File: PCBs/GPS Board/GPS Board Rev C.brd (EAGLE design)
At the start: 95.9 x 90.2 mm, 4 parts

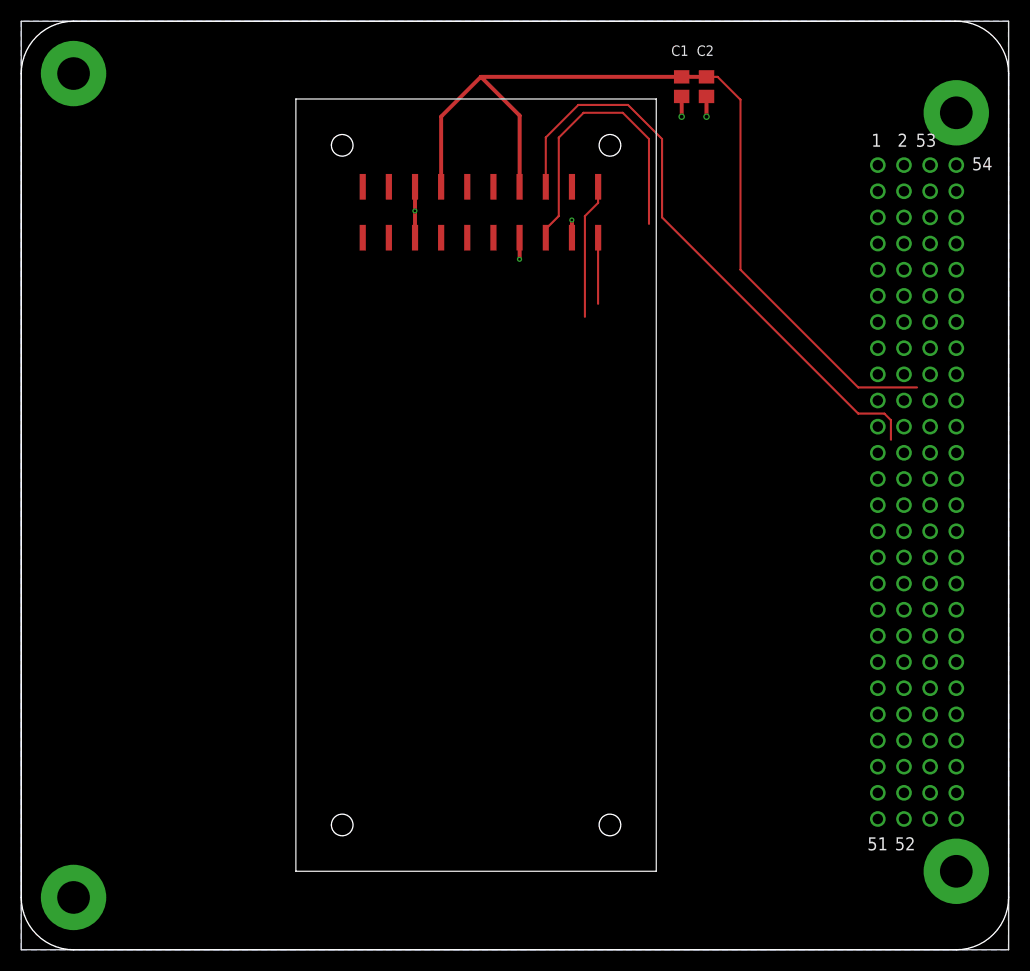
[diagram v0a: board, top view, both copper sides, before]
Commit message: Add test pads
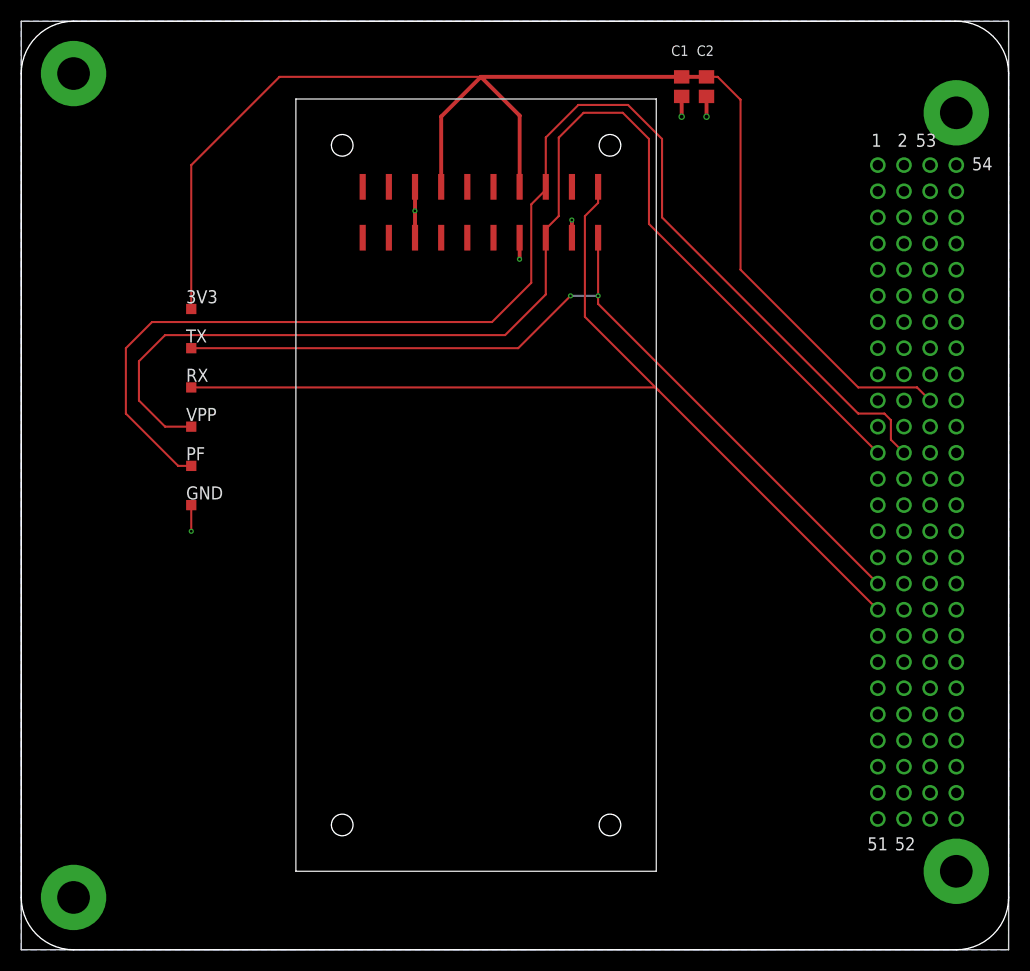
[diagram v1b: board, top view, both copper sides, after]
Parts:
- added 3V3, GND, PF, RX, TX, VPP: TPTP10SQ, testpad:TP10SQ
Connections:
- net GND: now also GND.TP
- net PF: now also PF.TP
- net RX: now also RX.TP
- net SW9: now also 3V3.TP
- net TX: now also TX.TP
- net VPP: now also VPP.TP
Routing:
- net VPP: track 29.3 -> 118.4 mm
- net RX: track 13.2 -> 98.9 mm
- net TX: track 6.43 -> 86.5 mm, vias 0 -> 2
- net PF: track 58.7 -> 127.2 mm
- net SW9: track 89.0 -> 136.5 mm
- net GND: track 12.7 -> 15.2 mm, vias 5 -> 6
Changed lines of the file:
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@@
 <element name="U$1" library="Cubesat" package="PINAV-L1" value="PINAV-L1" x="26.67" y="7.62"/>
 <element name="U$2" library="Cubesat" package="PC104_NO_DIMENSION" value="PC104_NO_DIMENSION" x="0" y="0"/>
+<element name="GND" library="testpad" library_urn="urn:adsk.eagle:library:385" package="TP10SQ" package3d_urn="urn:adsk.eagle:package:27962/1" value="TPTP10SQ" x="16.51" y="43.18">
+<attribute name="TP_SIGNAL_NAME" value="" x="16.51" y="43.18" size="1.778" layer="27" display="off"/>
+</element>
+<element name="TX" library="testpad" library_urn="urn:adsk.eagle:library:385" package="TP10SQ" package3d_urn="urn:adsk.eagle:package:27962/1" value="TPTP10SQ" x="16.51" y="58.42">
+<attribute name="TP_SIGNAL_NAME" value="" x="16.51" y="58.42" size="1.778" layer="27" display="off"/>
+</element>
+<element name="RX" library="testpad" library_urn="urn:adsk.eagle:library:385" package="TP10SQ" package3d_urn="urn:adsk.eagle:package:27962/1" value="TPTP10SQ" x="16.51" y="54.61">
+<attribute name="TP_SIGNAL_NAME" value="" x="16.51" y="54.61" size="1.778" layer="27" display="off"/>
+</element>
+<element name="3V3" library="testpad" library_urn="urn:adsk.eagle:library:385" package="TP10SQ" package3d_urn="urn:adsk.eagle:package:27962/1" value="TPTP10SQ" x="16.51" y="62.23">
+<attribute name="TP_SIGNAL_NAME" value="" x="16.51" y="62.23" size="1.778" layer="27" display="off"/>
+</element>
+<element name="VPP" library="testpad" library_urn="urn:adsk.eagle:library:385" package="TP10SQ" package3d_urn="urn:adsk.eagle:package:27962/1" value="TPTP10SQ" x="16.51" y="50.8">
+<attribute name="TP_SIGNAL_NAME" value="" x="16.51" y="50.8" size="1.778" layer="27" display="off"/>
+</element>
+<element name="PF" library="testpad" library_urn="urn:adsk.eagle:library:385" package="TP10SQ" package3d_urn="urn:adsk.eagle:package:27962/1" value="TPTP10SQ" x="16.51" y="46.99">
+<attribute name="TP_SIGNAL_NAME" value="" x="16.51" y="46.99" size="1.778" layer="27" display="off"/>
+</element>
 </elements>
 <signals>
@@
 <wire x1="86.995" y1="54.61" x2="81.28" y2="54.61" width="0.2032" layer="1"/>
 <contactref element="U$2" pad="71"/>
-<wire x1="88.265" y1="53.34" x2="86.995" y2="54.61" width="0" layer="19" extent="1-1"/>
+<wire x1="88.265" y1="53.34" x2="86.995" y2="54.61" width="0.2032" layer="1"/>
+<contactref element="3V3" pad="TP"/>
+<wire x1="44.638" y1="84.77" x2="25.08" y2="84.77" width="0.2032" layer="1"/>
+<wire x1="16.51" y1="76.2" x2="16.51" y2="62.23" width="0.2032" layer="1"/>
+<wire x1="25.08" y1="84.77" x2="16.51" y2="76.2" width="0.2032" layer="1"/>
 </signal>
 <signal name="GND">
@@
 <contactref element="U$2" pad="99"/>
 <contactref element="U$2" pad="100"/>
-<wire x1="64.135" y1="82.87" x2="66.548" y2="82.87" width="0" layer="19" extent="1-1"/>
-<wire x1="53.467" y1="70.866" x2="64.135" y2="80.899" width="0" layer="19" extent="1-1"/>
-<wire x1="48.4" y1="69.15" x2="53.48" y2="69.15" width="0" layer="19" extent="1-1"/>
-<wire x1="38.24" y1="69.15" x2="48.4" y2="69.15" width="0" layer="19" extent="1-1"/>
+<contactref element="GND" pad="TP"/>
+<wire x1="16.51" y1="43.18" x2="16.51" y2="40.64" width="0.2032" layer="1"/>
+<via x="16.51" y="40.64" extent="1-16" drill="0.254"/>
 <wire x1="38.227" y1="71.755" x2="38.24" y2="74.09" width="0" layer="19" extent="1-1"/>
-<wire x1="88.265" y1="66.04" x2="48.4" y2="67.069" width="0" layer="19" extent="1-1"/>
-<wire x1="90.805" y1="60.96" x2="88.265" y2="66.04" width="0" layer="19" extent="1-1"/>
-<wire x1="88.265" y1="55.88" x2="90.805" y2="60.96" width="0" layer="19" extent="1-1"/>
-<wire x1="88.265" y1="50.8" x2="88.265" y2="55.88" width="0" layer="19" extent="1-1"/>
-<wire x1="90.805" y1="50.8" x2="88.265" y2="50.8" width="0" layer="19" extent="1-1"/>
-<wire x1="90.805" y1="40.64" x2="90.805" y2="50.8" width="0" layer="19" extent="1-1"/>
-<wire x1="88.265" y1="40.64" x2="90.805" y2="40.64" width="0" layer="19" extent="1-1"/>
-<wire x1="90.805" y1="38.1" x2="90.805" y2="40.64" width="0" layer="19" extent="1-1"/>
-<wire x1="90.805" y1="17.78" x2="90.805" y2="38.1" width="0" layer="19" extent="1-1"/>
-<wire x1="88.265" y1="17.78" x2="90.805" y2="17.78" width="0" layer="19" extent="1-1"/>
 </signal>
 <signal name="VPP">
@@
 <wire x1="54.61" y1="81.28" x2="58.42" y2="81.28" width="0.2032" layer="1"/>
 <wire x1="58.42" y1="81.28" x2="60.96" y2="78.74" width="0.2032" layer="1"/>
-<wire x1="60.96" y1="78.74" x2="60.96" y2="70.485" width="0.2032" layer="1"/>
+<wire x1="60.96" y1="70.485" x2="60.96" y2="78.74" width="0.2032" layer="1"/>
 <wire x1="50.94" y1="69.99" x2="52.197" y2="71.247" width="0.2032" layer="1"/>
 <wire x1="52.197" y1="71.247" x2="52.197" y2="78.867" width="0.2032" layer="1"/>
 <wire x1="52.197" y1="78.867" x2="54.61" y2="81.28" width="0.2032" layer="1"/>
 <contactref element="U$2" pad="23"/>
-<wire x1="83.185" y1="48.26" x2="60.96" y2="70.485" width="0" layer="19" extent="1-1"/>
+<wire x1="83.185" y1="48.26" x2="60.96" y2="70.485" width="0.2032" layer="1"/>
+<contactref element="VPP" pad="TP"/>
+<wire x1="50.94" y1="69.15" x2="50.94" y2="63.64" width="0.2032" layer="1"/>
+<wire x1="50.94" y1="63.64" x2="46.99" y2="59.69" width="0.2032" layer="1"/>
+<wire x1="46.99" y1="59.69" x2="13.97" y2="59.69" width="0.2032" layer="1"/>
+<wire x1="13.97" y1="59.69" x2="11.43" y2="57.15" width="0.2032" layer="1"/>
+<wire x1="11.43" y1="53.34" x2="13.97" y2="50.8" width="0.2032" layer="1"/>
+<wire x1="13.97" y1="50.8" x2="16.51" y2="50.8" width="0.2032" layer="1"/>
+<wire x1="11.43" y1="57.15" x2="11.43" y2="53.34" width="0.2032" layer="1"/>
 </signal>
 <signal name="PF">
@@
 <wire x1="81.28" y1="52.07" x2="83.82" y2="52.07" width="0.2032" layer="1"/>
 <wire x1="83.82" y1="52.07" x2="84.455" y2="51.435" width="0.2032" layer="1"/>
-<wire x1="84.455" y1="51.435" x2="84.455" y2="49.53" width="0.2032" layer="1"/>
+<wire x1="84.455" y1="49.53" x2="84.455" y2="51.435" width="0.2032" layer="1"/>
 <wire x1="50.94" y1="78.88" x2="54.102" y2="82.042" width="0.2032" layer="1"/>
 <wire x1="54.102" y1="82.042" x2="58.928" y2="82.042" width="0.2032" layer="1"/>
@@
 <wire x1="62.23" y1="78.74" x2="62.23" y2="71.12" width="0.2032" layer="1"/>
 <contactref element="U$2" pad="24"/>
-<wire x1="85.725" y1="48.26" x2="84.455" y2="49.53" width="0" layer="19" extent="1-1"/>
+<wire x1="85.725" y1="48.26" x2="84.455" y2="49.53" width="0.2032" layer="1"/>
+<contactref element="PF" pad="TP"/>
+<wire x1="50.94" y1="74.09" x2="50.94" y2="73.8" width="0.2032" layer="1"/>
+<wire x1="50.94" y1="73.8" x2="49.53" y2="72.39" width="0.2032" layer="1"/>
+<wire x1="49.53" y1="64.77" x2="45.72" y2="60.96" width="0.2032" layer="1"/>
+<wire x1="12.7" y1="60.96" x2="10.16" y2="58.42" width="0.2032" layer="1"/>
+<wire x1="10.16" y1="58.42" x2="10.16" y2="52.07" width="0.2032" layer="1"/>
+<wire x1="10.16" y1="52.07" x2="15.24" y2="46.99" width="0.2032" layer="1"/>
+<wire x1="15.24" y1="46.99" x2="16.51" y2="46.99" width="0.2032" layer="1"/>
+<wire x1="49.53" y1="72.39" x2="49.53" y2="64.77" width="0.2032" layer="1"/>
+<wire x1="45.72" y1="60.96" x2="12.7" y2="60.96" width="0.2032" layer="1"/>
 </signal>
 <signal name="TX">
 <contactref element="U$1" pad="1"/>
-<wire x1="56.02" y1="69.15" x2="56.02" y2="62.725" width="0.2032" layer="1"/>
+<wire x1="56.02" y1="62.725" x2="56.02" y2="63.5" width="0.2032" layer="1"/>
 <contactref element="U$2" pad="33"/>
-<wire x1="83.185" y1="35.56" x2="56.02" y2="62.725" width="0" layer="19" extent="1-1"/>
+<wire x1="56.02" y1="63.5" x2="56.02" y2="69.15" width="0.2032" layer="1"/>
+<wire x1="83.185" y1="35.56" x2="56.02" y2="62.725" width="0.2032" layer="1"/>
+<contactref element="TX" pad="TP"/>
+<via x="56.02" y="63.5" extent="1-16" drill="0.254"/>
+<wire x1="56.02" y1="63.5" x2="53.34" y2="63.5" width="0.2032" layer="16"/>
+<via x="53.34" y="63.5" extent="1-16" drill="0.254"/>
+<wire x1="53.34" y1="63.5" x2="48.26" y2="58.42" width="0.2032" layer="1"/>
+<wire x1="48.26" y1="58.42" x2="16.51" y2="58.42" width="0.2032" layer="1"/>
 </signal>
 <signal name="RX">
@@
 <wire x1="56.02" y1="74.09" x2="56.02" y2="72.53" width="0.2032" layer="1"/>
 <wire x1="56.02" y1="72.53" x2="54.737" y2="71.247" width="0.2032" layer="1"/>
-<wire x1="54.737" y1="71.247" x2="54.737" y2="61.468" width="0.2032" layer="1"/>
+<wire x1="54.737" y1="61.468" x2="54.737" y2="71.247" width="0.2032" layer="1"/>
 <contactref element="U$2" pad="35"/>
-<wire x1="83.185" y1="33.02" x2="54.737" y2="61.468" width="0" layer="19" extent="1-1"/>
+<wire x1="83.185" y1="33.02" x2="61.9125" y2="54.2925" width="0.2032" layer="1"/>
+<contactref element="RX" pad="TP"/>
+<wire x1="61.9125" y1="54.2925" x2="54.737" y2="61.468" width="0.2032" layer="1"/>
+<wire x1="16.51" y1="54.61" x2="61.595" y2="54.61" width="0.2032" layer="1"/>
+<wire x1="61.595" y1="54.61" x2="61.9125" y2="54.2925" width="0.2032" layer="1"/>
 </signal>
 </signals>

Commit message: Rearrange pins to keep traces only on topside
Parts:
- moved PF 11.4 mm to (16.5, 58.4)
- moved TX 11.4 mm to (16.5, 47.0)
- moved RX 3.81 mm to (16.5, 50.8)
- moved VPP 3.81 mm to (16.5, 54.6)
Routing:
- net PF: track 127.2 -> 106.0 mm
- net VPP: track 118.4 -> 104.4 mm
- net RX: track 98.9 -> 106.1 mm
- net TX: track 86.5 -> 90.9 mm, vias 2 -> 0
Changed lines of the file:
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@@
 <setting verticaltext="up"/>
 </settings>
-<grid distance="50" unitdist="mil" unit="mil" style="lines" multiple="1" display="yes" altdistance="5" altunitdist="mil" altunit="mil"/>
+<grid distance="25" unitdist="mil" unit="mil" style="lines" multiple="1" display="yes" altdistance="5" altunitdist="mil" altunit="mil"/>
 <layers>
 <layer number="1" name="Top" color="4" fill="1" visible="yes" active="yes"/>
@@
 <layer number="43" name="vRestrict" color="2" fill="10" visible="yes" active="yes"/>
 <layer number="44" name="Drills" color="7" fill="1" visible="no" active="yes"/>
-<layer number="45" name="Holes" color="7" fill="1" visible="no" active="yes"/>
+<layer number="45" name="Holes" color="7" fill="1" visible="yes" active="yes"/>
 <layer number="46" name="Milling" color="3" fill="1" visible="no" active="yes"/>
 <layer number="47" name="Measures" color="7" fill="1" visible="no" active="yes"/>
@@
 <wire x1="0" y1="85.09" x2="5.08" y2="90.17" width="0.127" layer="20" curve="-90"/>
 <wire x1="5.08" y1="90.17" x2="90.678" y2="90.17" width="0.127" layer="20"/>
+<hole x="56.007" y="71.12" drill="0.35"/>
 </plain>
 <attributes>
@@
 <attribute name="TP_SIGNAL_NAME" value="" x="16.51" y="43.18" size="1.778" layer="27" display="off"/>
 </element>
-<element name="TX" library="testpad" library_urn="urn:adsk.eagle:library:385" package="TP10SQ" package3d_urn="urn:adsk.eagle:package:27962/1" value="TPTP10SQ" x="16.51" y="58.42">
-<attribute name="TP_SIGNAL_NAME" value="" x="16.51" y="58.42" size="1.778" layer="27" display="off"/>
-</element>
-<element name="RX" library="testpad" library_urn="urn:adsk.eagle:library:385" package="TP10SQ" package3d_urn="urn:adsk.eagle:package:27962/1" value="TPTP10SQ" x="16.51" y="54.61">
-<attribute name="TP_SIGNAL_NAME" value="" x="16.51" y="54.61" size="1.778" layer="27" display="off"/>
+<element name="TX" library="testpad" library_urn="urn:adsk.eagle:library:385" package="TP10SQ" package3d_urn="urn:adsk.eagle:package:27962/1" value="TPTP10SQ" x="16.51" y="46.99">
+<attribute name="TP_SIGNAL_NAME" value="" x="16.51" y="46.99" size="1.778" layer="27" display="off"/>
+</element>
+<element name="RX" library="testpad" library_urn="urn:adsk.eagle:library:385" package="TP10SQ" package3d_urn="urn:adsk.eagle:package:27962/1" value="TPTP10SQ" x="16.51" y="50.8">
+<attribute name="TP_SIGNAL_NAME" value="" x="16.51" y="50.8" size="1.778" layer="27" display="off"/>
 </element>
 <element name="3V3" library="testpad" library_urn="urn:adsk.eagle:library:385" package="TP10SQ" package3d_urn="urn:adsk.eagle:package:27962/1" value="TPTP10SQ" x="16.51" y="62.23">
 <attribute name="TP_SIGNAL_NAME" value="" x="16.51" y="62.23" size="1.778" layer="27" display="off"/>
 </element>
-<element name="VPP" library="testpad" library_urn="urn:adsk.eagle:library:385" package="TP10SQ" package3d_urn="urn:adsk.eagle:package:27962/1" value="TPTP10SQ" x="16.51" y="50.8">
-<attribute name="TP_SIGNAL_NAME" value="" x="16.51" y="50.8" size="1.778" layer="27" display="off"/>
-</element>
-<element name="PF" library="testpad" library_urn="urn:adsk.eagle:library:385" package="TP10SQ" package3d_urn="urn:adsk.eagle:package:27962/1" value="TPTP10SQ" x="16.51" y="46.99">
-<attribute name="TP_SIGNAL_NAME" value="" x="16.51" y="46.99" size="1.778" layer="27" display="off"/>
+<element name="VPP" library="testpad" library_urn="urn:adsk.eagle:library:385" package="TP10SQ" package3d_urn="urn:adsk.eagle:package:27962/1" value="TPTP10SQ" x="16.51" y="54.61">
+<attribute name="TP_SIGNAL_NAME" value="" x="16.51" y="54.61" size="1.778" layer="27" display="off"/>
+</element>
+<element name="PF" library="testpad" library_urn="urn:adsk.eagle:library:385" package="TP10SQ" package3d_urn="urn:adsk.eagle:package:27962/1" value="TPTP10SQ" x="16.51" y="58.42">
+<attribute name="TP_SIGNAL_NAME" value="" x="16.51" y="58.42" size="1.778" layer="27" display="off"/>
 </element>
 </elements>
@@
 <contactref element="VPP" pad="TP"/>
 <wire x1="50.94" y1="69.15" x2="50.94" y2="63.64" width="0.2032" layer="1"/>
-<wire x1="50.94" y1="63.64" x2="46.99" y2="59.69" width="0.2032" layer="1"/>
-<wire x1="46.99" y1="59.69" x2="13.97" y2="59.69" width="0.2032" layer="1"/>
-<wire x1="13.97" y1="59.69" x2="11.43" y2="57.15" width="0.2032" layer="1"/>
-<wire x1="11.43" y1="53.34" x2="13.97" y2="50.8" width="0.2032" layer="1"/>
-<wire x1="13.97" y1="50.8" x2="16.51" y2="50.8" width="0.2032" layer="1"/>
-<wire x1="11.43" y1="57.15" x2="11.43" y2="53.34" width="0.2032" layer="1"/>
+<wire x1="41.91" y1="54.61" x2="16.51" y2="54.61" width="0.2032" layer="1"/>
+<wire x1="50.94" y1="63.64" x2="41.91" y2="54.61" width="0.2032" layer="1"/>
 </signal>
 <signal name="PF">
@@
 <contactref element="PF" pad="TP"/>
 <wire x1="50.94" y1="74.09" x2="50.94" y2="73.8" width="0.2032" layer="1"/>
-<wire x1="50.94" y1="73.8" x2="49.53" y2="72.39" width="0.2032" layer="1"/>
-<wire x1="49.53" y1="64.77" x2="45.72" y2="60.96" width="0.2032" layer="1"/>
-<wire x1="12.7" y1="60.96" x2="10.16" y2="58.42" width="0.2032" layer="1"/>
-<wire x1="10.16" y1="58.42" x2="10.16" y2="52.07" width="0.2032" layer="1"/>
-<wire x1="10.16" y1="52.07" x2="15.24" y2="46.99" width="0.2032" layer="1"/>
-<wire x1="15.24" y1="46.99" x2="16.51" y2="46.99" width="0.2032" layer="1"/>
-<wire x1="49.53" y1="72.39" x2="49.53" y2="64.77" width="0.2032" layer="1"/>
-<wire x1="45.72" y1="60.96" x2="12.7" y2="60.96" width="0.2032" layer="1"/>
+<wire x1="50.94" y1="73.8" x2="47.117" y2="69.977" width="0.2032" layer="1"/>
+<wire x1="47.117" y1="69.977" x2="47.117" y2="62.357" width="0.2032" layer="1"/>
+<wire x1="43.18" y1="58.42" x2="16.51" y2="58.42" width="0.2032" layer="1"/>
+<wire x1="47.117" y1="62.357" x2="43.18" y2="58.42" width="0.2032" layer="1"/>
 </signal>
 <signal name="TX">
@@
 <wire x1="83.185" y1="35.56" x2="56.02" y2="62.725" width="0.2032" layer="1"/>
 <contactref element="TX" pad="TP"/>
-<via x="56.02" y="63.5" extent="1-16" drill="0.254"/>
-<wire x1="56.02" y1="63.5" x2="53.34" y2="63.5" width="0.2032" layer="16"/>
-<via x="53.34" y="63.5" extent="1-16" drill="0.254"/>
-<wire x1="53.34" y1="63.5" x2="48.26" y2="58.42" width="0.2032" layer="1"/>
-<wire x1="48.26" y1="58.42" x2="16.51" y2="58.42" width="0.2032" layer="1"/>
+<wire x1="56.02" y1="62.725" x2="40.285" y2="46.99" width="0.2032" layer="1"/>
+<wire x1="40.285" y1="46.99" x2="16.51" y2="46.99" width="0.2032" layer="1"/>
 </signal>
 <signal name="RX">
 <contactref element="U$1" pad="2"/>
-<wire x1="56.02" y1="74.09" x2="56.02" y2="72.53" width="0.2032" layer="1"/>
-<wire x1="56.02" y1="72.53" x2="54.737" y2="71.247" width="0.2032" layer="1"/>
-<wire x1="54.737" y1="61.468" x2="54.737" y2="71.247" width="0.2032" layer="1"/>
 <contactref element="U$2" pad="35"/>
-<wire x1="83.185" y1="33.02" x2="61.9125" y2="54.2925" width="0.2032" layer="1"/>
 <contactref element="RX" pad="TP"/>
-<wire x1="61.9125" y1="54.2925" x2="54.737" y2="61.468" width="0.2032" layer="1"/>
-<wire x1="16.51" y1="54.61" x2="61.595" y2="54.61" width="0.2032" layer="1"/>
-<wire x1="61.595" y1="54.61" x2="61.9125" y2="54.2925" width="0.2032" layer="1"/>
+<wire x1="56.02" y1="72.25" x2="60.325" y2="67.945" width="0.2032" layer="1"/>
+<wire x1="60.325" y1="67.945" x2="60.325" y2="60.96" width="0.2032" layer="1"/>
+<wire x1="60.325" y1="60.96" x2="81.915" y2="39.37" width="0.2032" layer="1"/>
+<wire x1="83.82" y1="39.37" x2="84.455" y2="38.735" width="0.2032" layer="1"/>
+<wire x1="84.455" y1="38.735" x2="84.455" y2="34.29" width="0.2032" layer="1"/>
+<wire x1="84.455" y1="34.29" x2="83.185" y2="33.02" width="0.2032" layer="1"/>
+<wire x1="56.02" y1="74.09" x2="56.02" y2="72.39" width="0.2032" layer="1"/>
+<wire x1="56.02" y1="72.39" x2="56.02" y2="72.25" width="0.2032" layer="1"/>
+<wire x1="81.915" y1="39.37" x2="83.82" y2="39.37" width="0.2032" layer="1"/>
+<wire x1="56.02" y1="72.25" x2="54.737" y2="70.967" width="0.2032" layer="1"/>
+<wire x1="40.005" y1="50.8" x2="16.51" y2="50.8" width="0.2032" layer="1"/>
+<wire x1="54.737" y1="70.967" x2="54.737" y2="65.532" width="0.2032" layer="1"/>
+<wire x1="54.737" y1="65.532" x2="40.005" y2="50.8" width="0.2032" layer="1"/>
 </signal>
 </signals>

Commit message: So. many. changes.
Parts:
- removed U$1: PINAV-L1, Cubesat:PINAV-L1
- added PINAV: (no value), Cubesat:PINAV-L1
- added PINAV-CONNECTOR: HLE-110-02-X-DV-BE-A, HLE-110-02-X-DV-BE-A:HLE-110-02-X-DV-BE-A
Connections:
- net GND: now also PINAV-CONNECTOR.15, PINAV-CONNECTOR.7; no longer U$1.15, U$1.16, U$1.3, U$1.7
- net PF: now also PINAV-CONNECTOR.6; no longer U$1.6
- net RX: now also PINAV-CONNECTOR.2; no longer U$1.2
- net SW9: now also PINAV-CONNECTOR.14, PINAV-CONNECTOR.8; no longer U$1.14, U$1.8
- net TX: now also PINAV-CONNECTOR.1; no longer U$1.1
- net VPP: now also PINAV-CONNECTOR.5; no longer U$1.5
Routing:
- net RX: track 106.1 -> 141.3 mm
- net GND: track 15.2 -> 12.5 mm, vias 6 -> 5
- net SW9: track 136.5 -> 134.0 mm
- net TX: track 90.9 -> 93.1 mm
- net VPP: track 104.4 -> 103.3 mm
